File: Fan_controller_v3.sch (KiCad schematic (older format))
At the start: 37 parts, among them J1 Load2, J2 Dig_mod_iface, K1 HFD2_005-S-L2-D_Split, K2 HFD2_005-S-L2-D_Split, Q1 BSS138, Q2 BSS138, U1 PCA9536DP

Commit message: Исправления в схеме и в печатной плате. Смещен вверх боковой конденсатор.
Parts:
- added C10, C8: 100nF, Capacitor_SMD:C_0603_1608Metric, symbol Device:C_Small
- added Q1, Q2, Q5, Q6: 2N5551S, Package_TO_SOT_SMD:SOT-23, symbol Device:Q_NPN_BEC
- added R1, R13, R14, R2: 1k, Resistor_SMD:R_0603_1608Metric, symbol Device:R_Small
- added R15, R16, R3, R4: 20k, Resistor_SMD:R_0603_1608Metric, symbol Device:R_Small
- added U1: ADuM1251ARZ, Package_SO:SOIC-8_3.9x4.9mm_P1.27mm, symbol Modules:ADuM1251ARZ
- J1: footprint Connector_PinHeader_2.54mm:PinHeader_1x02_P2.54mm_Horizontal -> Modules:PinHeader_1x03_P2.54mm; symbol Connector_Generic:Conn_01x02 -> Connector_Generic:Conn_01x03
- R5: renamed from R1; value 210 -> 47
- renumbered C5 to C1, C3 to C11, C4 to C12, C7 to C13, C6 to C2, C1 to C3, C2 to C4, C8 to C5, C9 to C6, C10 to C7, C11 to C9, Q1 to Q3, Q2 to Q4, R6 to R10, R3 to R17, R4 to R18, R7 to R19, R8 to R20, R2 to R6, R9 to R7, R10 to R8, R5 to R9, U1 to U2
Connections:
- net +5VL is gone; now on net +5VP: D1.1 (K), D2.1 (K), D3.1 (K), D4.1 (K), JP1.2 (B), K1.1, K1.2, K2.1, K2.2
- net GND is gone; now on net GND2: U2.4 (VSS)
- net +5VP: now also C10.2, U1.8 (VDD2); no longer C1.1, C2.2, J2.1 (Pin_1), J2.2 (Pin_2), PS1.2 (+Vin), Q3.1 (G), Q4.1 (G), R11.2, R12.2, R7.2, R8.2
- net GND1: now also C8.1, U1.4 (GND1); no longer C13.2
- net GND2: now also C13.2, C10.1, Q1.2 (E), Q2.2 (E), Q5.2 (E), Q6.2 (E), R15.2, R16.2, R3.2, R4.2, U1.5 (GND2)
- net I2C_SCL: now also U1.6 (SCL2); no longer Q4.2 (S), R12.1
- net I2C_SDA: now also U1.7 (SDA2); no longer Q3.2 (S), R11.1
- net K1_rst: now also U2.1 (IO0), R2.2; no longer U2.2 (IO1)
- net K1_set: now also U2.2 (IO1), R1.2; no longer U2.1 (IO0)
- net K2_rst: now also U2.3 (IO2), R14.2; no longer U2.5 (IO3)
- net K2_set: now also U2.5 (IO3), R13.2; no longer U2.3 (IO2)
- net at C7.2, K1.11, K2.11: now also C5.2; no longer C5.1
- net at K1.4: now also C5.1; no longer C5.2
- net at K2.4: now also J1.3 (Pin_3); no longer J1.2 (Pin_2)
- net K1_rst_drv/Drv_openC: no longer names the net of R6.1
- net K1_rst_drv/Drv_openC: now also Q2.3 (C)
- net K1_set_drv/Drv_openC: no longer names the net of R5.1
- net K1_set_drv/Drv_openC: now also Q1.3 (C)
- net K2_rst_drv/Drv_openC: no longer names the net of R18.1
- net K2_rst_drv/Drv_openC: now also Q6.3 (C)
- net K2_set_drv/Drv_openC: no longer names the net of R17.1
- net K2_set_drv/Drv_openC: now also Q5.3 (C)
- new net: Q3.2 (S), R11.1, U1.2 (SDA1)
- new net: Q4.2 (S), R12.1, U1.3 (SCL1)
- new net: Q1.1 (B), R1.1, R3.1
- new net: Q2.1 (B), R2.1, R4.1
- new net: Q5.1 (B), R13.1, R15.1
- new net: Q6.1 (B), R14.1, R16.1
- new net +5P: C1.1, C2.2, C8.2, J2.1 (Pin_1), J2.2 (Pin_2), PS1.2 (+Vin), Q3.1 (G), Q4.1 (G), R11.2, R12.2, R7.2, R8.2, U1.1 (VDD1)
- no-connect marks 4 -> 1
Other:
- moved on the sheet: C1, C11, C12, C13, C2, C3, C4, C5, C6, C7, C9, D1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

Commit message: Добавлены недостающие компоненты схемы. Закончена трассировка платы.
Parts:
- J2: footprint Connector_PinSocket_1.27mm:PinSocket_2x05_P1.27mm_Horizontal -> Connector_PinSocket_1.27mm:PinSocket_2x03_P1.27mm_Horizontal; symbol Connector_Generic:Conn_02x05_Odd_Even -> Connector_Generic:Conn_02x03_Odd_Even
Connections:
- net GND1: no longer J2.10 (Pin_10), J2.9 (Pin_9)
- net scl0: now also J2.6 (Pin_6); no longer J2.7 (Pin_7), J2.8 (Pin_8)
- net sda0: no longer J2.6 (Pin_6)
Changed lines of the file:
@@
 	5075 2225 5425 2225
 Wire Wire Line
-	950  2725 1550 2725
-Wire Wire Line
-	1550 2725 1550 2700
-$Comp
-L Connector_Generic:Conn_02x05_Odd_Even J?
-U 1 1 616E418D
-P 1200 2450
-AR Path="/611899F2/616E418D" Ref="J?"  Part="1"
-AR Path="/616E418D" Ref="J2"  Part="1"
-AR Path="/61554169/616E418D" Ref="J?"  Part="1"
-AR Path="/616C9C69/61554169/616E418D" Ref="J?"  Part="1"
-AR Path="/619FB8A8/616E418D" Ref="J?"  Part="1"
-F 0 "J2" H 1250 2750 50  0000 C CNN
-F 1 "Dig_mod_iface" H 1250 2125 50  0000 C CNN
-F 2 "Connector_PinSocket_1.27mm:PinSocket_2x05_P1.27mm_Horizontal" H 1200 2450 50  0001 C CNN
-F 3 "~" H 1200 2450 50  0001 C CNN
-	1    1200 2450
-	1    0    0    -1
-$EndComp
-Wire Wire Line
 	1750 2300 1825 2300
-Text Label 800  2550 0    50   ~ 0
-scl0
-Text Label 800  2450 0    50   ~ 0
-sda0
-Wire Wire Line
-	800  2550 1000 2550
-Wire Wire Line
-	800  2450 1000 2450
 Text Label 1525 2550 0    50   ~ 0
 scl0
@@
 sda0
 Wire Wire Line
-	1550 2650 1500 2650
-Wire Wire Line
-	950  2650 950  2725
-Wire Wire Line
-	1000 2650 950  2650
-Wire Wire Line
-	1000 2350 850  2350
-Wire Wire Line
 	1750 2450 1750 2300
 Wire Wire Line
@@
 	1975 2550 1825 2550
 Wire Wire Line
-	1825 2550 1500 2550
+	1825 2550 950  2550
 Wire Wire Line
 	2475 2875 2175 2875
@@
 Text Label 4725 2475 2    50   ~ 0
 I2C_SCL
-$Comp
-L power:GND1 #PWR?
-U 1 1 61CB7628
-P 1575 2700
-AR Path="/6118243C/61CB7628" Ref="#PWR?"  Part="1"
-AR Path="/61CB7628" Ref="#PWR08"  Part="1"
-AR Path="/61553E5D/61CB7628" Ref="#PWR?"  Part="1"
-AR Path="/61554169/61CB7628" Ref="#PWR?"  Part="1"
-AR Path="/616C9C69/61554169/61CB7628" Ref="#PWR?"  Part="1"
-AR Path="/619FB8A8/61CB7628" Ref="#PWR?"  Part="1"
-F 0 "#PWR08" H 1575 2450 50  0001 C CNN
-F 1 "GND1" V 1475 2625 50  0000 C CNN
-F 2 "" H 1575 2700 50  0001 C CNN
-F 3 "" H 1575 2700 50  0001 C CNN
-	1    1575 2700
-	0    -1   1    0
-$EndComp
-Wire Wire Line
-	1575 2700 1550 2700
-Connection ~ 1550 2700
-Wire Wire Line
-	1550 2700 1550 2650
 Wire Wire Line
 	3000 2175 3050 2175
@@
 Wire Wire Line
 	4250 4925 4250 4875
+Wire Wire Line
+	950  2550 950  2450
+Wire Wire Line
+	950  2450 1000 2450
+Wire Wire Line
+	1000 2350 850  2350
+$Comp
+L Connector_Generic:Conn_02x03_Odd_Even J?
+U 1 1 616E418D
+P 1300 2350
+AR Path="/611899F2/616E418D" Ref="J?"  Part="1"
+AR Path="/616E418D" Ref="J2"  Part="1"
+AR Path="/61554169/616E418D" Ref="J?"  Part="1"
+AR Path="/616C9C69/61554169/616E418D" Ref="J?"  Part="1"
+AR Path="/619FB8A8/616E418D" Ref="J?"  Part="1"
+F 0 "J2" H 1350 2550 50  0000 C CNN
+F 1 "Dig_mod_iface" H 1350 2100 50  0000 C CNN
+F 2 "Connector_PinSocket_1.27mm:PinSocket_2x03_P1.27mm_Horizontal" H 1300 2350 50  0001 C CNN
+F 3 "~" H 1300 2350 50  0001 C CNN
+	1    1300 2350
+	-1   0    0    -1
+$EndComp
 $EndSCHEMATC

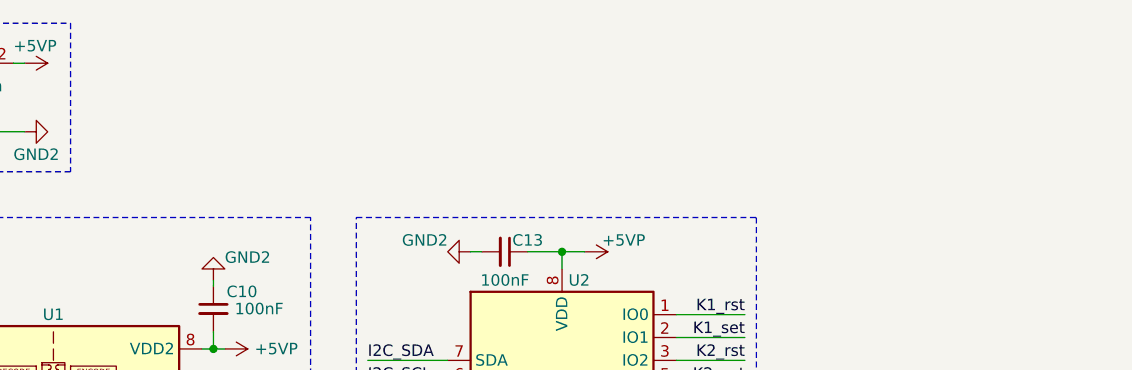
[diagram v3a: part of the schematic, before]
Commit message: Добавил изолирующие отверстия на схему. Подправил компоненты отверстий. Удалил контуры отверстий на обеих слоях платы.
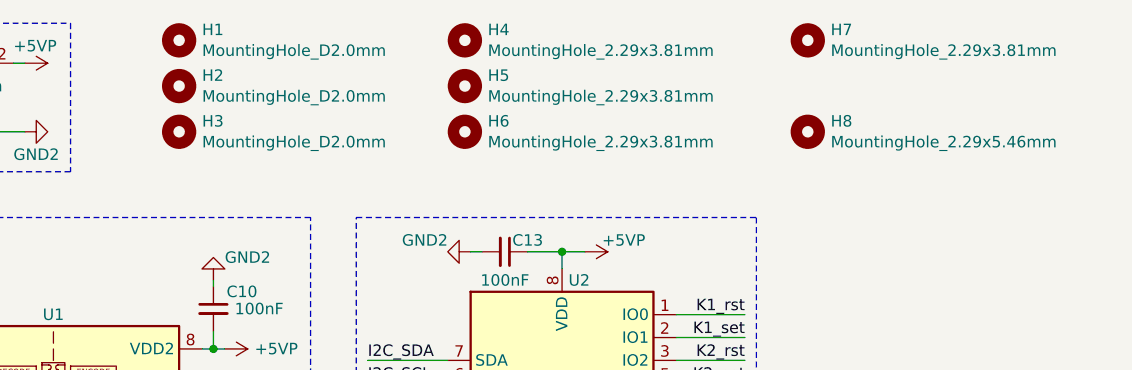
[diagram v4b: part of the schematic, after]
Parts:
- added H1, H2, H3: MountingHole_D2.0mm, Modules:MountingHole_D2.0mm, symbol Mechanical:MountingHole
- added H4, H5, H6, H7: MountingHole_2.29x3.81mm, Modules:MountingHole_2.29x3.81mm, symbol Mechanical:MountingHole
- added H8: MountingHole_2.29x5.46mm, Modules:MountingHole_2.29x5.46mm, symbol Mechanical:MountingHole
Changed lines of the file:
@@
 	-1   0    0    -1
 $EndComp
+$Comp
+L Mechanical:MountingHole H1
+U 1 1 61EE5E54
+P 4250 825
+F 0 "H1" H 4350 871 50  0000 L CNN
+F 1 "MountingHole_D2.0mm" H 4350 780 50  0000 L CNN
+F 2 "Modules:MountingHole_D2.0mm" H 4250 825 50  0001 C CNN
+F 3 "~" H 4250 825 50  0001 C CNN
+	1    4250 825
+	1    0    0    -1
+$EndComp
+$Comp
+L Mechanical:MountingHole H2
+U 1 1 61EF235E
+P 4250 1025
+F 0 "H2" H 4350 1071 50  0000 L CNN
+F 1 "MountingHole_D2.0mm" H 4350 980 50  0000 L CNN
+F 2 "Modules:MountingHole_D2.0mm" H 4250 1025 50  0001 C CNN
+F 3 "~" H 4250 1025 50  0001 C CNN
+	1    4250 1025
+	1    0    0    -1
+$EndComp
+$Comp
+L Mechanical:MountingHole H3
+U 1 1 61EF275B
+P 4250 1225
+F 0 "H3" H 4350 1271 50  0000 L CNN
+F 1 "MountingHole_D2.0mm" H 4350 1180 50  0000 L CNN
+F 2 "Modules:MountingHole_D2.0mm" H 4250 1225 50  0001 C CNN
+F 3 "~" H 4250 1225 50  0001 C CNN
+	1    4250 1225
+	1    0    0    -1
+$EndComp
+$Comp
+L Mechanical:MountingHole H8
+U 1 1 61EF2AAD
+P 7000 1225
+F 0 "H8" H 7100 1271 50  0000 L CNN
+F 1 "MountingHole_2.29x5.46mm" H 7100 1180 50  0000 L CNN
+F 2 "Modules:MountingHole_2.29x5.46mm" H 7000 1225 50  0001 C CNN
+F 3 "~" H 7000 1225 50  0001 C CNN
+	1    7000 1225
+	1    0    0    -1
+$EndComp
+$Comp
+L Mechanical:MountingHole H4
+U 1 1 61EF389C
+P 5500 825
+F 0 "H4" H 5600 871 50  0000 L CNN
+F 1 "MountingHole_2.29x3.81mm" H 5600 780 50  0000 L CNN
+F 2 "Modules:MountingHole_2.29x3.81mm" H 5500 825 50  0001 C CNN
+F 3 "~" H 5500 825 50  0001 C CNN
+	1    5500 825
+	1    0    0    -1
+$EndComp
+$Comp
+L Mechanical:MountingHole H5
+U 1 1 61EF3C50
+P 5500 1025
+F 0 "H5" H 5600 1071 50  0000 L CNN
+F 1 "MountingHole_2.29x3.81mm" H 5600 980 50  0000 L CNN
+F 2 "Modules:MountingHole_2.29x3.81mm" H 5500 1025 50  0001 C CNN
+F 3 "~" H 5500 1025 50  0001 C CNN
+	1    5500 1025
+	1    0    0    -1
+$EndComp
+$Comp
+L Mechanical:MountingHole H6
+U 1 1 61F0529C
+P 5500 1225
+F 0 "H6" H 5600 1271 50  0000 L CNN
+F 1 "MountingHole_2.29x3.81mm" H 5600 1180 50  0000 L CNN
+F 2 "Modules:MountingHole_2.29x3.81mm" H 5500 1225 50  0001 C CNN
+F 3 "~" H 5500 1225 50  0001 C CNN
+	1    5500 1225
+	1    0    0    -1
+$EndComp
+$Comp
+L Mechanical:MountingHole H7
+U 1 1 61F12FF9
+P 7000 825
+F 0 "H7" H 7100 871 50  0000 L CNN
+F 1 "MountingHole_2.29x3.81mm" H 7100 780 50  0000 L CNN
+F 2 "Modules:MountingHole_2.29x3.81mm" H 7000 825 50  0001 C CNN
+F 3 "~" H 7000 825 50  0001 C CNN
+	1    7000 825
+	1    0    0    -1
+$EndComp
 $EndSCHEMATC
